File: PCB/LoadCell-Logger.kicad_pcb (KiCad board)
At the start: 2 copper layers, 100 x 100 mm, 71 parts, among them CN1 LoadCell, CN2 LoadCell, CN3 LoadCell, CN4 LoadCell, J1 Debug, J2 Debug_Power, J3 Debug_XH, Q1 MMBT3906, Q2 MMBT3906, Q3 MMBT3906, Q4 MMBT3906, SW1 User, SW2 Reset, SW3 SW_SPDT, U1 Pico, U2 TC74HCU04AF, U3 HX711, U4 HX711, U5 HX711, U6 HX711, U7 Pico, Y1 13.824MHz

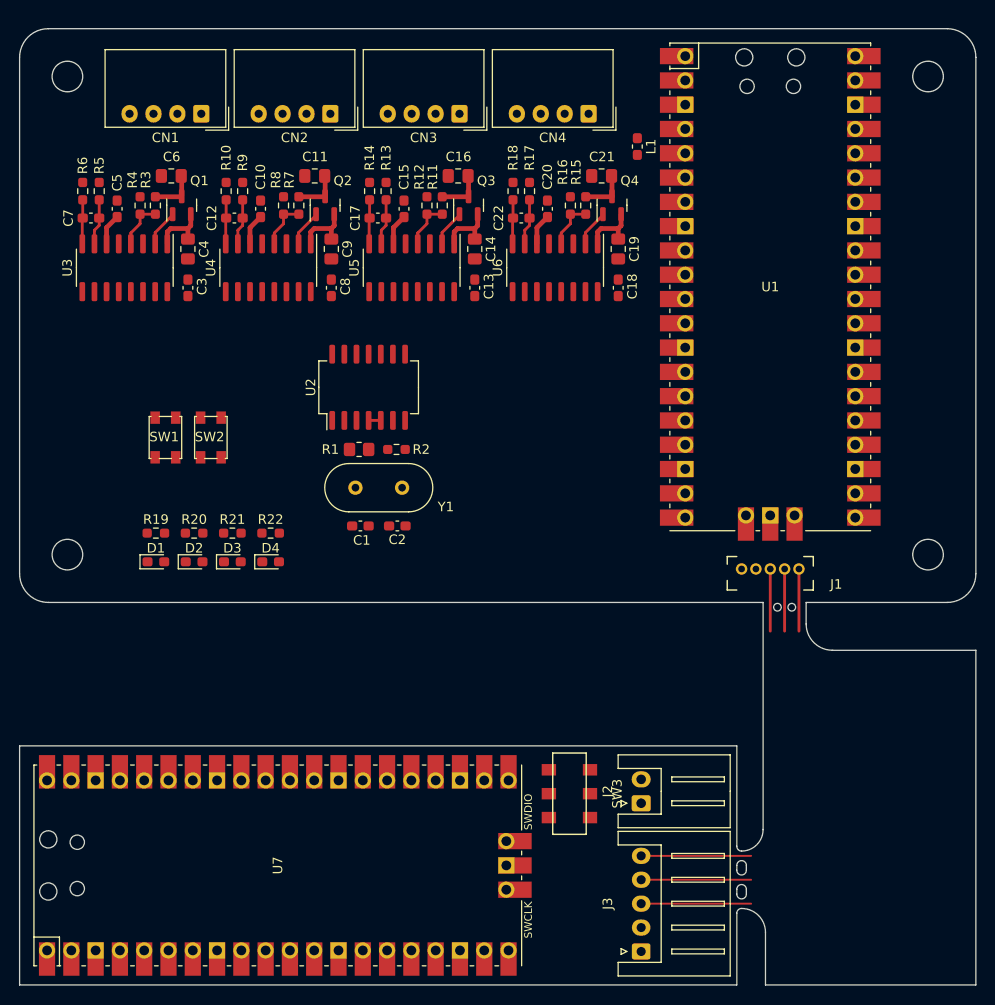
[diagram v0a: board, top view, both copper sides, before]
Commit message: ロガー側配線完了
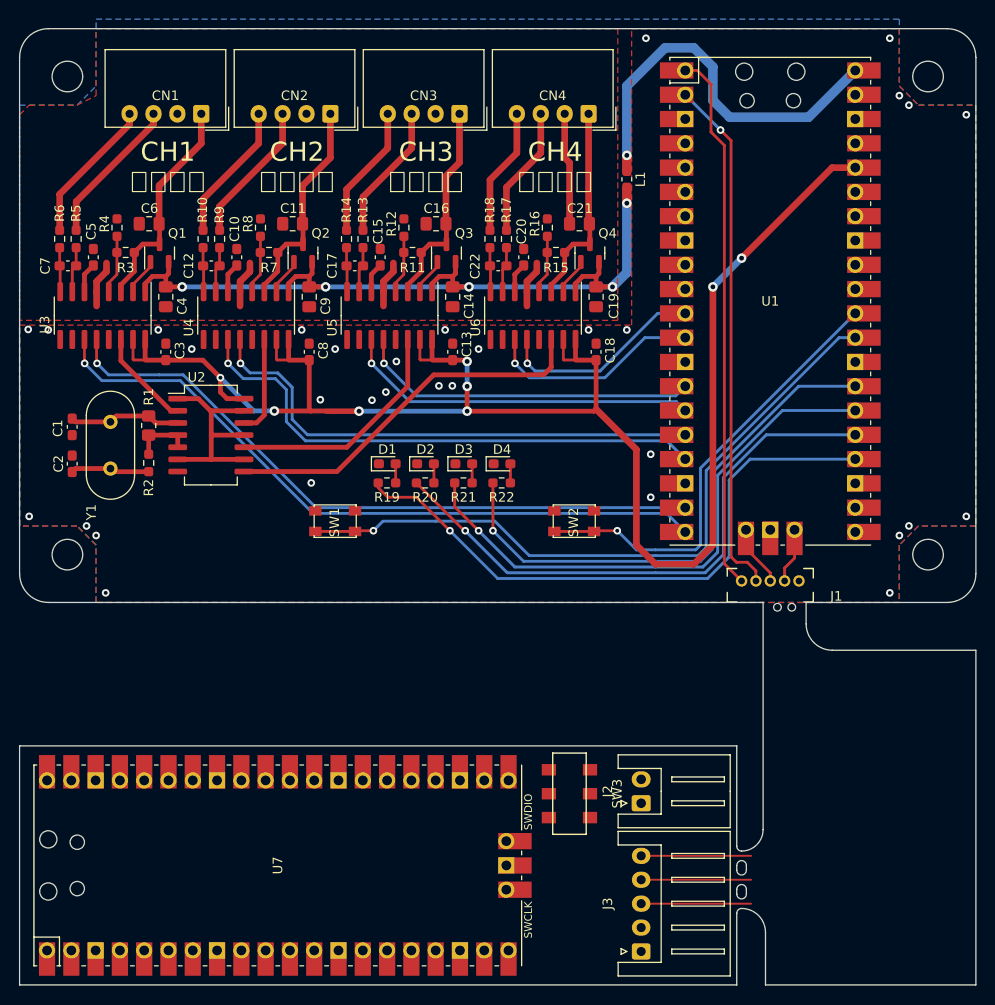
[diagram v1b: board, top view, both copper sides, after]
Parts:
- moved SW2 39.0 mm to (108.0, 101.5), turned to 180 degrees
- moved C2 34.6 mm to (55.5, 95.5), turned to 90 degrees
- moved C1 31.9 mm to (55.5, 91.6), turned to -90 degrees
- moved Y1 26.5 mm to (59.5, 91.1), turned to -90 degrees
- moved D1 26.3 mm to (88.5, 95.5)
- moved D2 26.3 mm to (92.5, 95.5)
- moved D3 26.3 mm to (96.5, 95.5)
- moved D4 26.3 mm to (100.5, 95.5)
- moved R2 26.0 mm to (63.5, 95.4), turned to 90 degrees
- moved R19 24.7 mm to (88.4, 97.5)
- moved R20 24.7 mm to (92.4, 97.5)
- moved R21 24.7 mm to (96.4, 97.5)
- moved R22 24.7 mm to (100.4, 97.5)
- moved R1 22.1 mm to (63.5, 91.5), turned to -90 degrees
- moved SW1 19.8 mm to (83.0, 101.5), turned to 180 degrees
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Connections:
- C10 pad 2: GNDA -> GND
- C11 pad 1: GNDA -> GND
- C14 pad 2: GNDA -> GND
- C15 pad 2: GNDA -> GND
- C16 pad 1: GNDA -> GND
- C19 pad 2: GNDA -> GND
- C20 pad 2: GNDA -> GND
- C21 pad 1: GNDA -> GND
- C4 pad 2: GNDA -> GND
- C5 pad 2: GNDA -> GND
- C6 pad 1: GNDA -> GND
- C9 pad 2: GNDA -> GND
- CN1 pad 2: GNDA -> GND
- CN2 pad 2: GNDA -> GND
- CN3 pad 2: GNDA -> GND
- CN4 pad 2: GNDA -> GND
- R12 pad 2: GNDA -> GND
- R16 pad 2: GNDA -> GND
- R4 pad 2: GNDA -> GND
- R8 pad 2: GNDA -> GND
- U1 pad 11: /DATA1 -> /DATA4
- U1 pad 12: /SCK1 -> /SCK4
- U1 pad 14: /DATA2 -> /DATA3
- U1 pad 15: /SCK2 -> /SCK3
- U1 pad 16: /DATA3 -> /DATA2
- U1 pad 17: /SCK3 -> /SCK2
- U1 pad 19: /DATA4 -> /DATA1
- U1 pad 20: /SCK4 -> /SCK1
- U2 pad 12: /CLK4 -> /CLK2
- U2 pad 8: /CLK2 -> /CLK4
- U3 pad 5: GNDA -> GND
- U4 pad 5: GNDA -> GND
- U5 pad 5: GNDA -> GND
- U6 pad 5: GNDA -> GND
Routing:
- net +3V3: track 0.00 -> 175.3 mm, vias 0 -> 8
- net /SCK1: track 0.00 -> 72.6 mm, vias 0 -> 1
- net Net-(SW1-Pad1): track 0.00 -> 72.6 mm, vias 0 -> 1
- net /DATA1: track 0.00 -> 70.3 mm, vias 0 -> 1
- net Net-(U1-Pad24): track 0.00 -> 64.2 mm, vias 0 -> 1
- net +5VA: track 25.1 -> 87.0 mm, vias 0 -> 5
- net Net-(R20-Pad1): track 0.00 -> 60.5 mm, vias 0 -> 1
- net Net-(R21-Pad1): track 0.00 -> 58.5 mm, vias 0 -> 1
- net /TX: track 0.00 -> 56.6 mm
- net Net-(R22-Pad1): track 0.00 -> 56.5 mm, vias 0 -> 1
- net /SCK2: track 0.00 -> 56.4 mm, vias 0 -> 1
- net /RX: track 0.00 -> 54.6 mm, vias 0 -> 1
- net /DATA2: track 0.00 -> 54.1 mm, vias 0 -> 1
- net Net-(SW2-Pad1): track 0.00 -> 47.3 mm, vias 0 -> 1
- net +5V: track 0.00 -> 41.5 mm, vias 0 -> 1
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- added copper zone on B.Cu, net GND
- added copper zone on F.Cu, net GND
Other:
- board text added: "CH1 緑白黒赤"
- board text added: "CH2 緑白黒赤"
- board text added: "CH3 緑白黒赤"
- board text added: "CH4 緑白黒赤"

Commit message: 基板設計完了
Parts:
- added SW3: Reset, user:SKRPACE010_kai, F.Cu at (145.0, 77.8)
- SW1: value User -> A
- SW2: value Reset -> B
- moved SW1 1.33 mm to (81.7, 101.5)
- moved SW4 1.17 mm to (108.1, 131.0), turned to -90 degrees
- renumbered SW3 to SW4
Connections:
- J1 pad 3: /SWCLK -> /CLK
- J1 pad 4: /SWDIO -> /DIO
- SW2 pad 1: Net-(SW2-Pad1) -> Net-(U1-Pad31)
- U1 pad 30: Net-(SW2-Pad1) -> Net-(U1-Pad30)
- U1 pad 31: unconnected-(U1-Pad31) -> Net-(U1-Pad31)
- U1 pad 41: /SWCLK -> /CLK
- U1 pad 43: /SWDIO -> /DIO
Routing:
- net /CLK: track 0.00 -> 111.8 mm, vias 0 -> 3
- net /DIO: track 0.00 -> 106.9 mm
- net Net-(SW4-Pad3): track 0.00 -> 60.3 mm
- net /Pico->MCU: track 0.00 -> 51.4 mm
- net Net-(U1-Pad31): track 0.00 -> 50.2 mm, vias 0 -> 1
- net Net-(SW4-Pad1): track 0.00 -> 50.0 mm
- net /Pico<-MCU: track 0.00 -> 49.1 mm
- net Net-(SW2-Pad1): track 47.3 -> 0.00 mm, vias 1 -> 0
- net GND: track 31.4 -> 48.9 mm, vias 32 -> 61
- net Net-(U1-Pad30): track 0.00 -> 10.7 mm
- net Net-(J2-Pad1): track 0.00 -> 9.05 mm
- net /SWCLK: track 6.40 -> 0.00 mm
- net /SWDIO: track 5.78 -> 0.00 mm
- net Net-(SW1-Pad1): track 72.6 -> 73.9 mm
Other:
- board text added: "- +"
- board text added: "4ch LoadCell Logger"
- board text added: "A"
- board text added: "B"
- board text added: "GND DIO CLK TX> RX<"
- board text added: "Reset"
- board text added: "v1.0 2022.04.28 @n_yosihisa"
- board text added: "←3.3V 5V→"

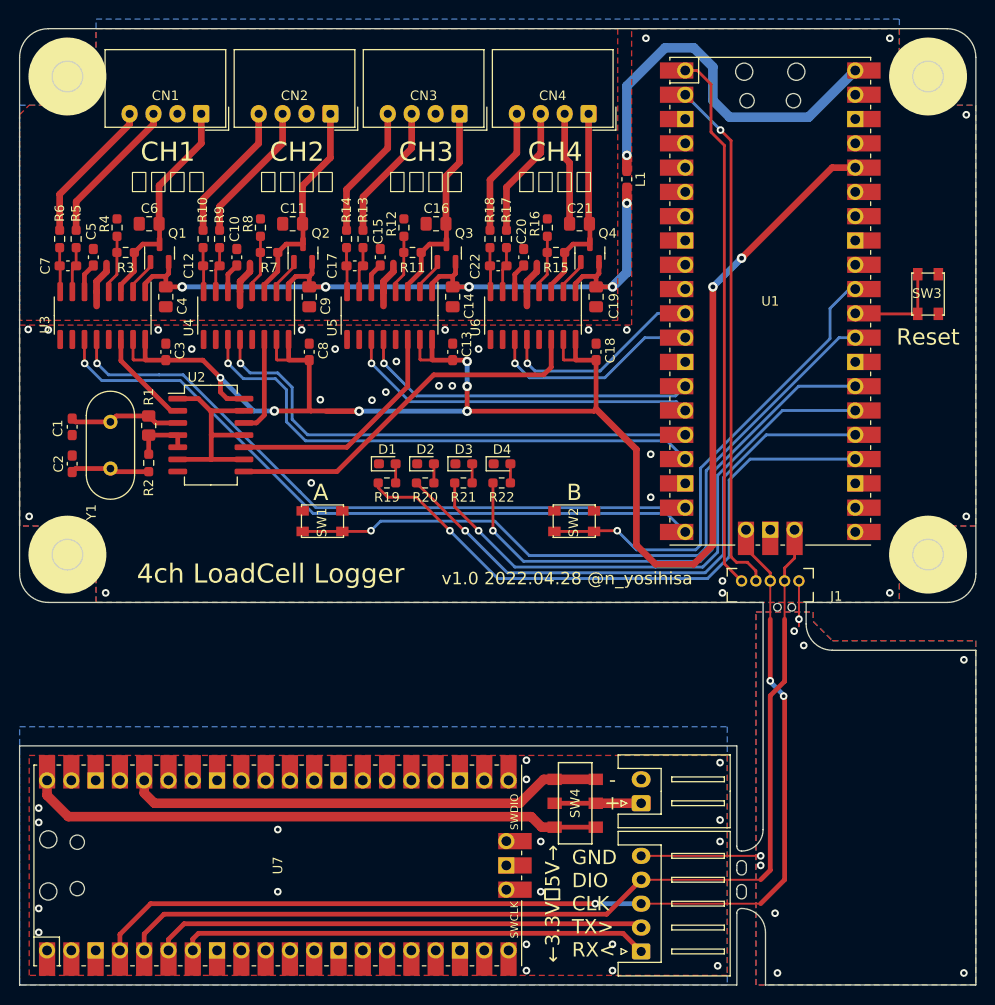
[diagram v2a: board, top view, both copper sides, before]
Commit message: デバッガー削除
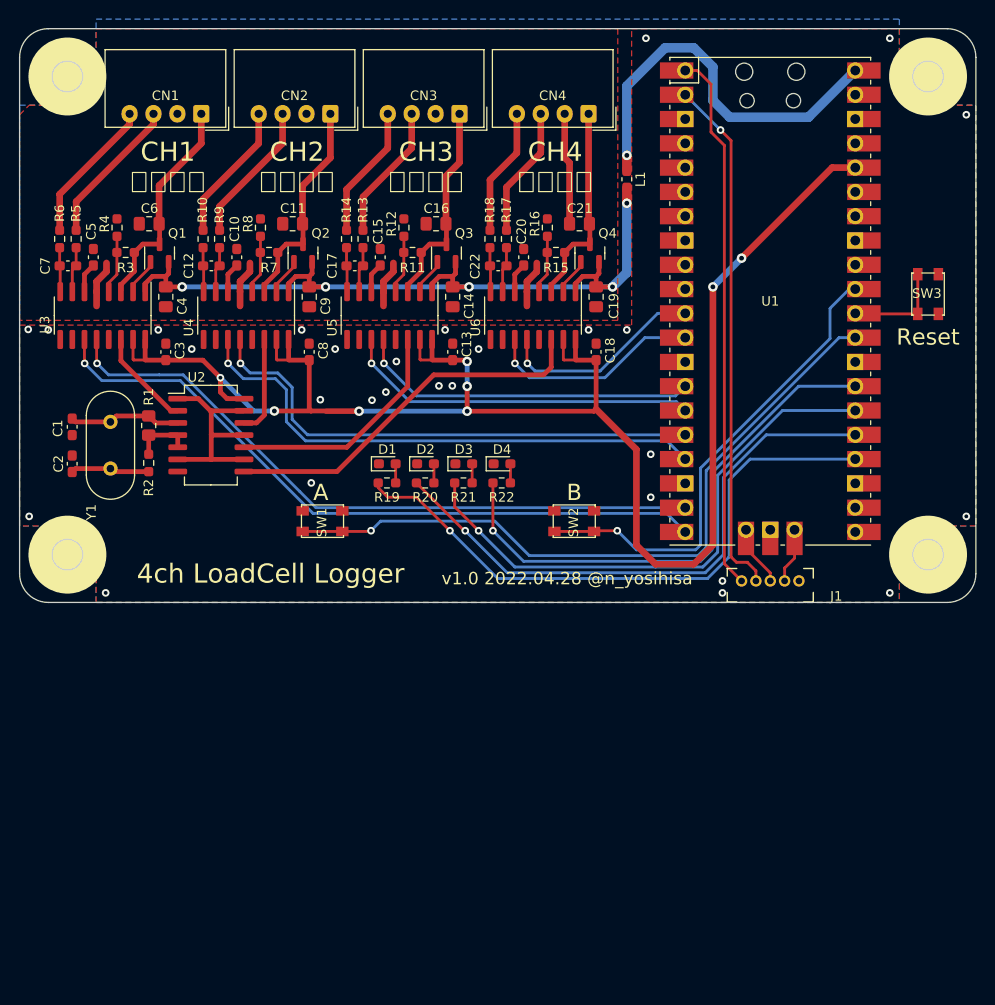
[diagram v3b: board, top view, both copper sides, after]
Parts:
- removed J2: Debug_Power, Connector_JST:JST_XH_S2B-XH-A_1x02_P2.50mm_Horizontal
- removed J3: Debug_XH, Connector_JST:JST_XH_S5B-XH-A_1x05_P2.50mm_Horizontal
- removed SW4: SW_SPDT, user:SSSS213202_parallel
- removed U7: Pico, MCU_RaspberryPi_and_Boards:RPi_Pico_SMD_TH
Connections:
- net /CLK renamed /SWCLK
- net /DIO renamed /SWDIO
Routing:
- net /SWCLK: track 111.8 -> 6.40 mm, vias 3 -> 0
- net /SWDIO: track 106.9 -> 5.78 mm
- net Net-(SW4-Pad3): track 60.3 -> 0.00 mm
- net /Pico->MCU: track 51.4 -> 0.00 mm
- net Net-(SW4-Pad1): track 50.0 -> 0.00 mm
- net /Pico<-MCU: track 49.1 -> 0.00 mm
- net GND: track 48.9 -> 31.4 mm, vias 61 -> 34
- net Net-(J2-Pad1): track 9.05 -> 0.00 mm
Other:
- board size 100 x 100 mm -> 100 x 60 mm
- board text removed: "- +"
- board text removed: "GND DIO CLK TX> RX<"
- board text removed: "←3.3V 5V→"
